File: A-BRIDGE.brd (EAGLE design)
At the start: 44.8 x 20.3 mm, 10 parts, among them IC1 74HC240DW, IC2 A4950, IC3 A4950

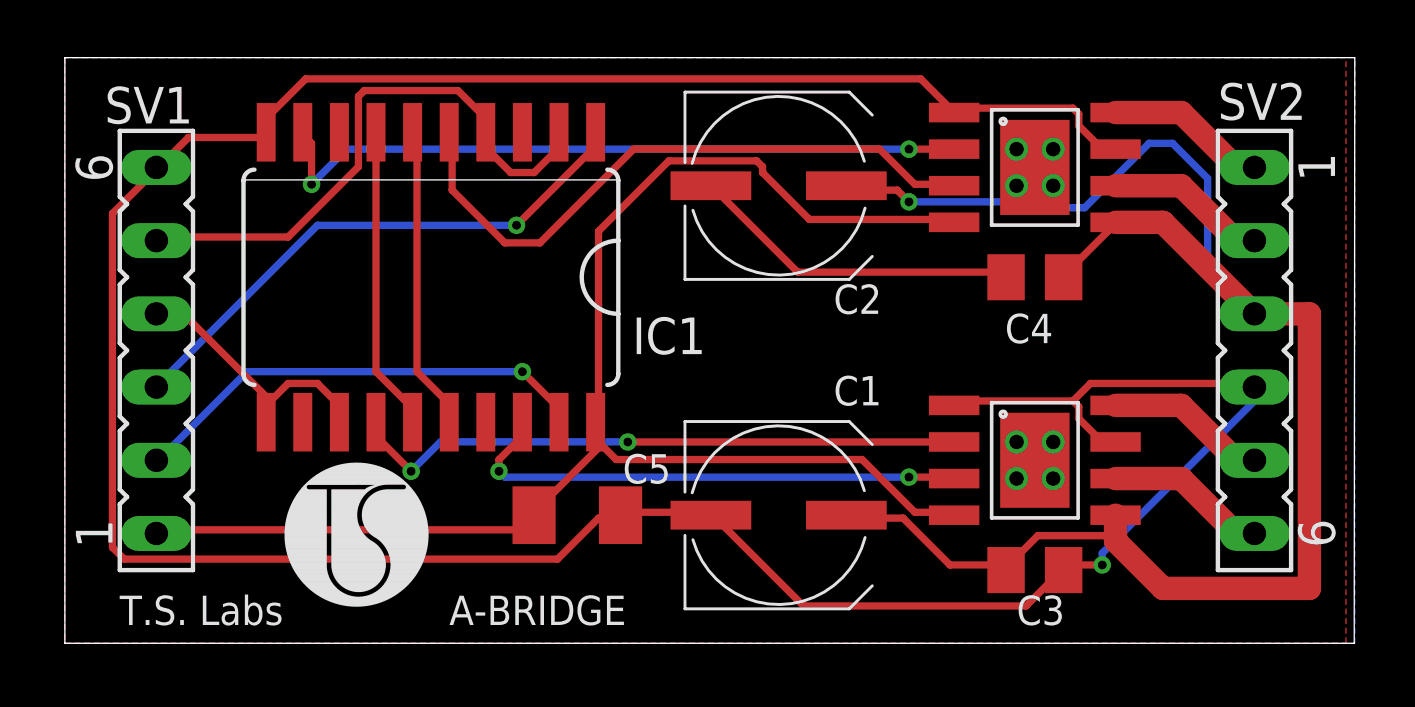
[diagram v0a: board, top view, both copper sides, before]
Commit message: A-BRIDGE rev.2
Added silkscreen pinout
Fixed grounding problems
Better Heat dissipation
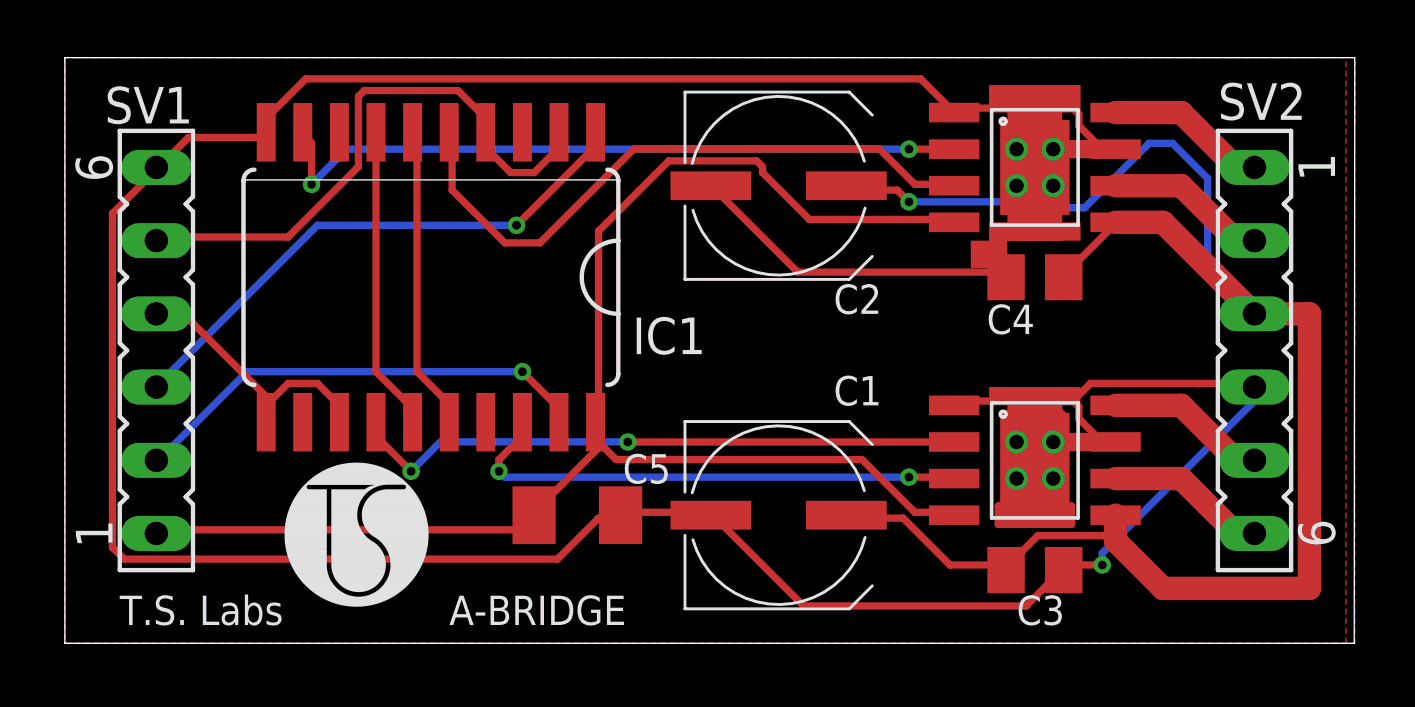
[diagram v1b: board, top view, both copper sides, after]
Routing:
- net N$1: track 0.00 -> 6.35 mm
- net N$2: track 0.00 -> 4.07 mm
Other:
- board text added: "+5V"
- board text added: "A-BRIDGE rev.2"
- board text added: "EN1"
- board text added: "EN2"
- board text added: "GND"
- board text added: "OUT1A"
- board text added: "OUT1B"
- board text added: "OUT2A"
- board text added: "OUT2B"
- board text added: "PWM1"
- board text added: "PWM2"
- board text added: "VMOT"

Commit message: rev2.01
Added "hot surface" warning
Better heat dissipation on bottom area
Bigger capacitor's footprint for hand soldering
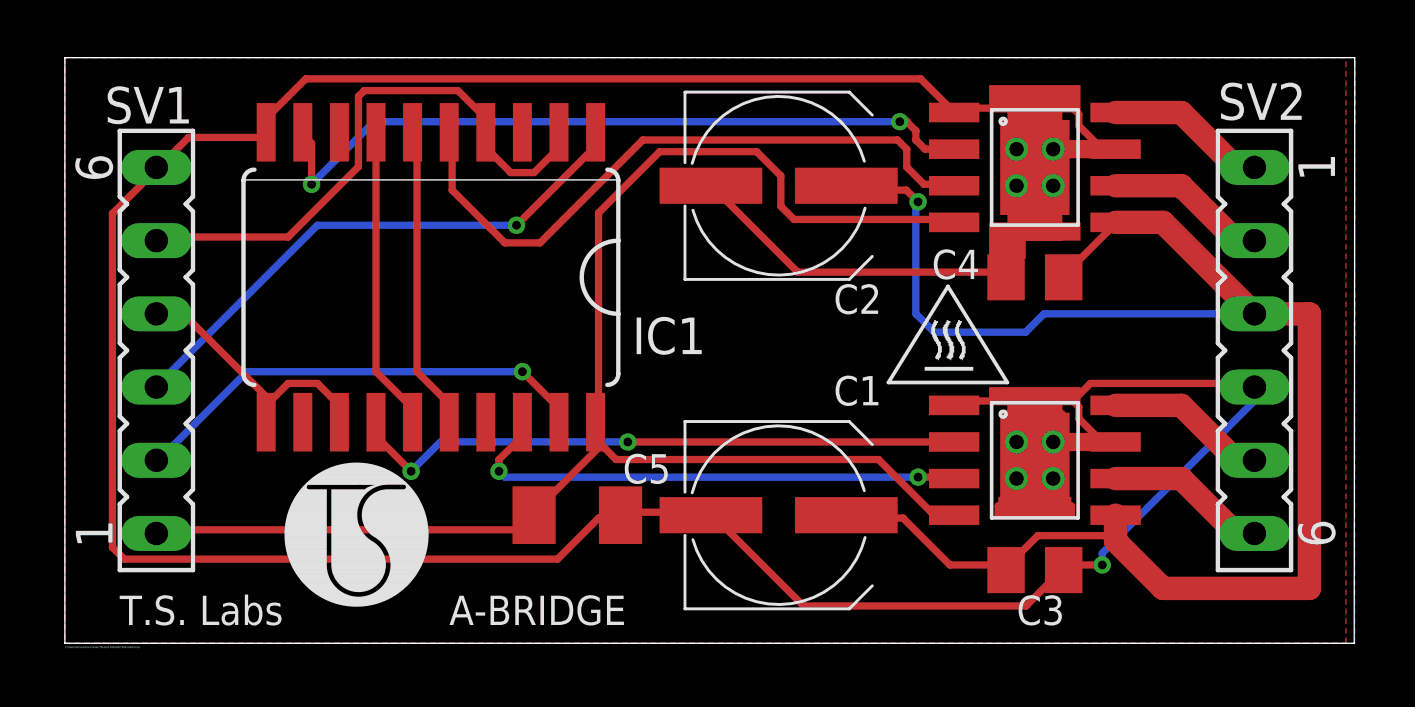
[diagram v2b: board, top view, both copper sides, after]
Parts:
- C1, C2: device rcl:UD-6,3X7,7_NICHICON -> rcl:UD-6,3X7,7_NICHICON_HS
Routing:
- net +5V: track 52.6 -> 53.8 mm
- net N$14: track 24.7 -> 25.7 mm
- net VCC: track 58.9 -> 58.2 mm
- net N$1: track 6.35 -> 5.71 mm
- net N$15: track 22.1 -> 22.7 mm
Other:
- board text added: "C:/Users/Simone/Documents/TSLabs/LOGO/Altri/5041(Hot).bmp"
